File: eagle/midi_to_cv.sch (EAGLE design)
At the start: 49 parts, among them IC1 TL084P, IC2 TL084P, U1 ATMEGA328P_PDIP

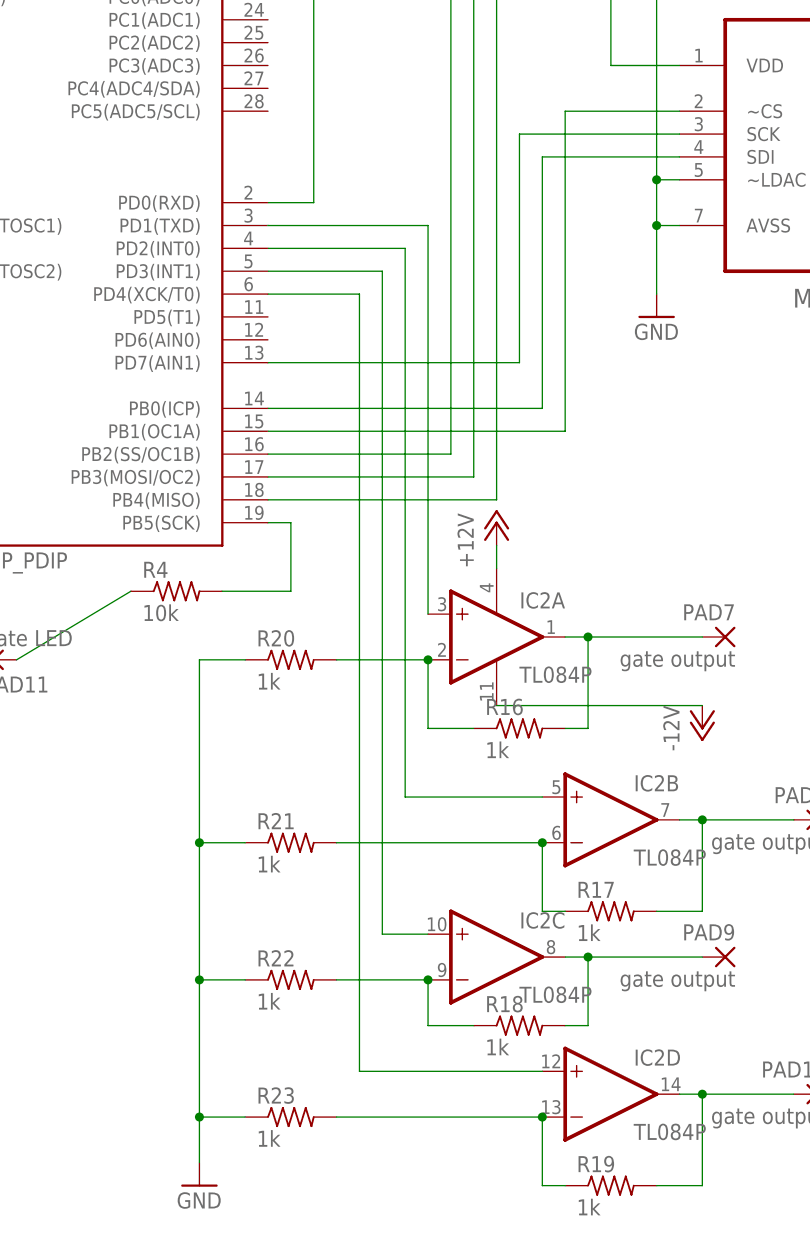
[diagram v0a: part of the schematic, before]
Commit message: routed with jumpers for gates and one via
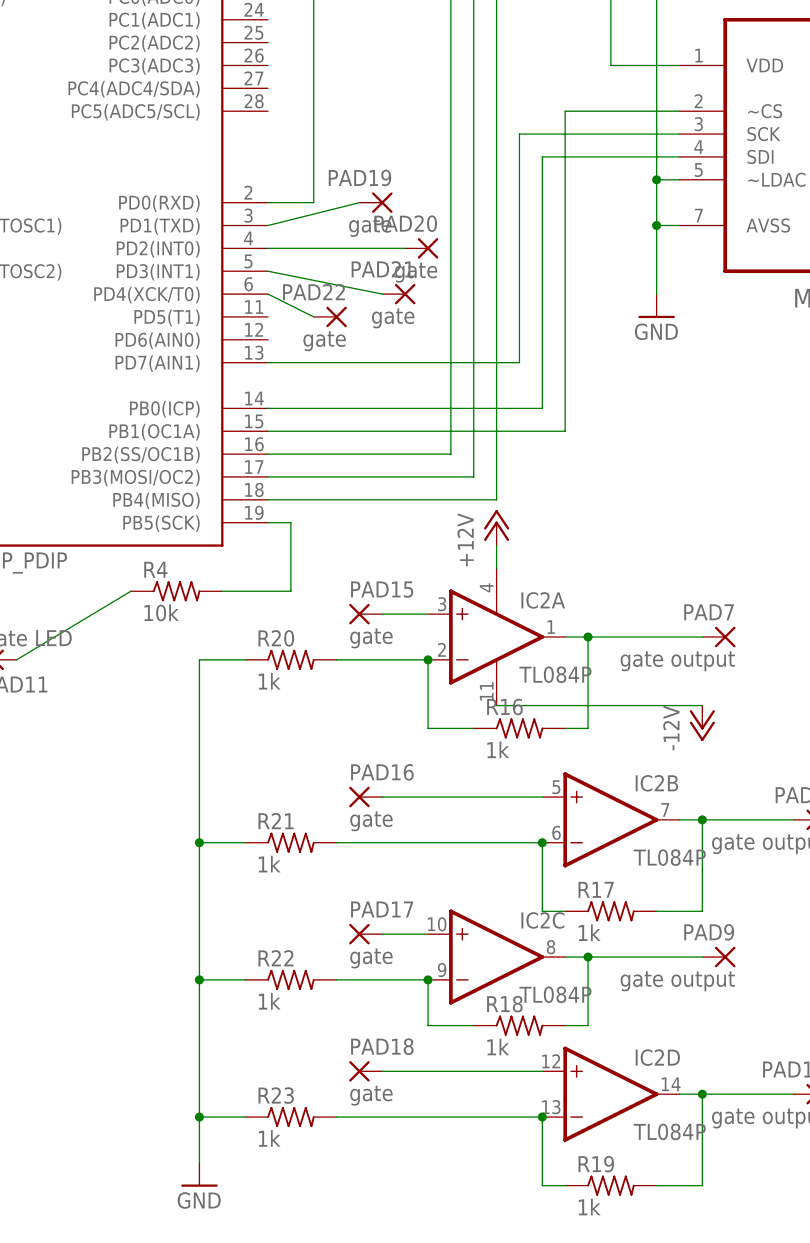
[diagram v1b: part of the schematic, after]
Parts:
- added PAD15, PAD16, PAD17, PAD18, PAD19, PAD20, PAD21, PAD22: gate, wirepad:2,54/0,9
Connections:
- new net N$43: PAD22.P, U1.PD4(XCK/T0)
- new net N$44: IC2C.+IN, PAD17.P
- new net N$45: IC2B.+IN, PAD16.P
- new net N$46: IC2A.+IN, PAD15.P
- net N$31: now also PAD19.P; no longer IC2A.+IN
- net N$32: now also PAD20.P; no longer IC2B.+IN
- net N$33: now also PAD21.P; no longer IC2C.+IN
- net N$34: now also PAD18.P; no longer U1.PD4(XCK/T0)
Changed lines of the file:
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@@
 <grid distance="0.1" unitdist="inch" unit="inch" style="lines" multiple="1" display="no" altdistance="0.01" altunitdist="inch" altunit="inch"/>
 <layers>
-<layer number="1" name="Top" color="4" fill="1" visible="yes" active="no"/>
-<layer number="16" name="Bottom" color="1" fill="1" visible="yes" active="no"/>
-<layer number="17" name="Pads" color="2" fill="1" visible="yes" active="no"/>
-<layer number="18" name="Vias" color="2" fill="1" visible="yes" active="no"/>
-<layer number="19" name="Unrouted" color="6" fill="1" visible="yes" active="no"/>
-<layer number="20" name="Dimension" color="15" fill="1" visible="yes" active="no"/>
-<layer number="21" name="tPlace" color="7" fill="1" visible="yes" active="no"/>
-<layer number="22" name="bPlace" color="7" fill="1" visible="yes" active="no"/>
-<layer number="23" name="tOrigins" color="15" fill="1" visible="yes" active="no"/>
-<layer number="24" name="bOrigins" color="15" fill="1" visible="yes" active="no"/>
-<layer number="25" name="tNames" color="7" fill="1" visible="yes" active="no"/>
-<layer number="26" name="bNames" color="7" fill="1" visible="yes" active="no"/>
-<layer number="27" name="tValues" color="7" fill="1" visible="yes" active="no"/>
-<layer number="28" name="bValues" color="7" fill="1" visible="yes" active="no"/>
+<layer number="1" name="Top" color="4" fill="1" visible="no" active="no"/>
+<layer number="16" name="Bottom" color="1" fill="1" visible="no" active="no"/>
+<layer number="17" name="Pads" color="2" fill="1" visible="no" active="no"/>
+<layer number="18" name="Vias" color="2" fill="1" visible="no" active="no"/>
+<layer number="19" name="Unrouted" color="6" fill="1" visible="no" active="no"/>
+<layer number="20" name="Dimension" color="15" fill="1" visible="no" active="no"/>
+<layer number="21" name="tPlace" color="7" fill="1" visible="no" active="no"/>
+<layer number="22" name="bPlace" color="7" fill="1" visible="no" active="no"/>
+<layer number="23" name="tOrigins" color="15" fill="1" visible="no" active="no"/>
+<layer number="24" name="bOrigins" color="15" fill="1" visible="no" active="no"/>
+<layer number="25" name="tNames" color="7" fill="1" visible="no" active="no"/>
+<layer number="26" name="bNames" color="7" fill="1" visible="no" active="no"/>
+<layer number="27" name="tValues" color="7" fill="1" visible="no" active="no"/>
+<layer number="28" name="bValues" color="7" fill="1" visible="no" active="no"/>
 <layer number="29" name="tStop" color="7" fill="3" visible="no" active="no"/>
 <layer number="30" name="bStop" color="7" fill="6" visible="no" active="no"/>
@@
 <layer number="35" name="tGlue" color="7" fill="4" visible="no" active="no"/>
 <layer number="36" name="bGlue" color="7" fill="5" visible="no" active="no"/>
-<layer number="37" name="tTest" color="7" fill="1" visible="yes" active="no"/>
-<layer number="38" name="bTest" color="7" fill="1" visible="yes" active="no"/>
+<layer number="37" name="tTest" color="7" fill="1" visible="no" active="no"/>
+<layer number="38" name="bTest" color="7" fill="1" visible="no" active="no"/>
 <layer number="39" name="tKeepout" color="4" fill="11" visible="no" active="no"/>
 <layer number="40" name="bKeepout" color="1" fill="11" visible="no" active="no"/>
@@
 <layer number="44" name="Drills" color="7" fill="1" visible="no" active="no"/>
 <layer number="45" name="Holes" color="7" fill="1" visible="no" active="no"/>
-<layer number="46" name="Milling" color="3" fill="1" visible="yes" active="no"/>
-<layer number="47" name="Measures" color="7" fill="1" visible="yes" active="no"/>
-<layer number="48" name="Document" color="7" fill="1" visible="yes" active="no"/>
-<layer number="49" name="Reference" color="7" fill="1" visible="yes" active="no"/>
-<layer number="50" name="dxf" color="7" fill="1" visible="yes" active="no"/>
-<layer number="51" name="tDocu" color="7" fill="1" visible="yes" active="no"/>
-<layer number="52" name="bDocu" color="7" fill="1" visible="yes" active="no"/>
-<layer number="53" name="tGND_GNDA" color="7" fill="9" visible="yes" active="no"/>
-<layer number="54" name="bGND_GNDA" color="1" fill="9" visible="yes" active="no"/>
-<layer number="56" name="wert" color="7" fill="1" visible="yes" active="no"/>
-<layer number="57" name="tCAD" color="7" fill="1" visible="yes" active="no"/>
+<layer number="46" name="Milling" color="3" fill="1" visible="no" active="no"/>
+<layer number="47" name="Measures" color="7" fill="1" visible="no" active="no"/>
+<layer number="48" name="Document" color="7" fill="1" visible="no" active="no"/>
+<layer number="49" name="Reference" color="7" fill="1" visible="no" active="no"/>
+<layer number="50" name="dxf" color="7" fill="1" visible="no" active="no"/>
+<layer number="51" name="tDocu" color="7" fill="1" visible="no" active="no"/>
+<layer number="52" name="bDocu" color="7" fill="1" visible="no" active="no"/>
+<layer number="53" name="tGND_GNDA" color="7" fill="9" visible="no" active="no"/>
+<layer number="54" name="bGND_GNDA" color="1" fill="9" visible="no" active="no"/>
+<layer number="56" name="wert" color="7" fill="1" visible="no" active="no"/>
+<layer number="57" name="tCAD" color="7" fill="1" visible="no" active="no"/>
 <layer number="90" name="Modules" color="5" fill="1" visible="yes" active="yes"/>
 <layer number="91" name="Nets" color="2" fill="1" visible="yes" active="yes"/>
@@
 <part name="P+7" library="supply1" deviceset="+12V" device=""/>
 <part name="P+8" library="supply1" deviceset="+12V" device=""/>
+<part name="PAD15" library="wirepad" deviceset="2,54/0,9" device="" value="gate"/>
+<part name="PAD16" library="wirepad" deviceset="2,54/0,9" device="" value="gate"/>
+<part name="PAD17" library="wirepad" deviceset="2,54/0,9" device="" value="gate"/>
+<part name="PAD18" library="wirepad" deviceset="2,54/0,9" device="" value="gate"/>
+<part name="PAD19" library="wirepad" deviceset="2,54/0,9" device="" value="gate"/>
+<part name="PAD20" library="wirepad" deviceset="2,54/0,9" device="" value="gate"/>
+<part name="PAD21" library="wirepad" deviceset="2,54/0,9" device="" value="gate"/>
+<part name="PAD22" library="wirepad" deviceset="2,54/0,9" device="" value="gate"/>
 </parts>
 <sheets>
@@
 <instance part="P+8" gate="1" x="68.58" y="15.24"/>
 <instance part="IC2" gate="P" x="68.58" y="2.54"/>
+<instance part="PAD15" gate="1" x="53.34" y="5.08"/>
+<instance part="PAD16" gate="1" x="53.34" y="-15.24"/>
+<instance part="PAD17" gate="1" x="53.34" y="-30.48"/>
+<instance part="PAD18" gate="1" x="53.34" y="-45.72"/>
+<instance part="PAD19" gate="1" x="55.88" y="50.8" rot="MR0"/>
+<instance part="PAD20" gate="1" x="60.96" y="45.72" rot="MR0"/>
+<instance part="PAD21" gate="1" x="58.42" y="40.64" rot="MR0"/>
+<instance part="PAD22" gate="1" x="50.8" y="38.1" rot="MR0"/>
 </instances>
 <busses>
@@
 <segment>
 <pinref part="U1" gate="G$1" pin="PD1(TXD)"/>
-<pinref part="IC2" gate="A" pin="+IN"/>
-<wire x1="43.18" y1="48.26" x2="60.96" y2="48.26" width="0.1524" layer="91"/>
-<wire x1="60.96" y1="48.26" x2="60.96" y2="5.08" width="0.1524" layer="91"/>
+<wire x1="43.18" y1="48.26" x2="53.34" y2="50.8" width="0.1524" layer="91"/>
+<pinref part="PAD19" gate="1" pin="P"/>
 </segment>
 </net>
@@
 <pinref part="U1" gate="G$1" pin="PD2(INT0)"/>
 <wire x1="43.18" y1="45.72" x2="58.42" y2="45.72" width="0.1524" layer="91"/>
-<wire x1="58.42" y1="45.72" x2="58.42" y2="-15.24" width="0.1524" layer="91"/>
-<pinref part="IC2" gate="B" pin="+IN"/>
-<wire x1="58.42" y1="-15.24" x2="73.66" y2="-15.24" width="0.1524" layer="91"/>
+<pinref part="PAD20" gate="1" pin="P"/>
 </segment>
 </net>
@@
 <segment>
 <pinref part="U1" gate="G$1" pin="PD3(INT1)"/>
-<wire x1="43.18" y1="43.18" x2="55.88" y2="43.18" width="0.1524" layer="91"/>
-<wire x1="55.88" y1="43.18" x2="55.88" y2="-30.48" width="0.1524" layer="91"/>
-<pinref part="IC2" gate="C" pin="+IN"/>
-<wire x1="55.88" y1="-30.48" x2="60.96" y2="-30.48" width="0.1524" layer="91"/>
+<wire x1="43.18" y1="43.18" x2="55.88" y2="40.64" width="0.1524" layer="91"/>
+<pinref part="PAD21" gate="1" pin="P"/>
 </segment>
 </net>
 <net name="N$34" class="0">
 <segment>
-<pinref part="U1" gate="G$1" pin="PD4(XCK/T0)"/>
-<wire x1="43.18" y1="40.64" x2="53.34" y2="40.64" width="0.1524" layer="91"/>
-<wire x1="53.34" y1="40.64" x2="53.34" y2="-45.72" width="0.1524" layer="91"/>
 <pinref part="IC2" gate="D" pin="+IN"/>
-<wire x1="53.34" y1="-45.72" x2="73.66" y2="-45.72" width="0.1524" layer="91"/>
+<wire x1="55.88" y1="-45.72" x2="73.66" y2="-45.72" width="0.1524" layer="91"/>
+<pinref part="PAD18" gate="1" pin="P"/>
 </segment>
 </net>
@@
 </segment>
 </net>
+<net name="N$43" class="0">
+<segment>
+<pinref part="U1" gate="G$1" pin="PD4(XCK/T0)"/>
+<wire x1="43.18" y1="40.64" x2="48.26" y2="38.1" width="0.1524" layer="91"/>
+<pinref part="PAD22" gate="1" pin="P"/>
+</segment>
+</net>
+<net name="N$44" class="0">
+<segment>
+<pinref part="IC2" gate="C" pin="+IN"/>
+<wire x1="55.88" y1="-30.48" x2="60.96" y2="-30.48" width="0.1524" layer="91"/>
+<pinref part="PAD17" gate="1" pin="P"/>
+</segment>
+</net>
+<net name="N$45" class="0">
+<segment>
+<pinref part="IC2" gate="B" pin="+IN"/>
+<wire x1="55.88" y1="-15.24" x2="73.66" y2="-15.24" width="0.1524" layer="91"/>
+<pinref part="PAD16" gate="1" pin="P"/>
+</segment>
+</net>
+<net name="N$46" class="0">
+<segment>
+<pinref part="PAD15" gate="1" pin="P"/>
+<pinref part="IC2" gate="A" pin="+IN"/>
+<wire x1="55.88" y1="5.08" x2="60.96" y2="5.08" width="0.1524" layer="91"/>
+</segment>
+</net>

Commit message: corrected to smaller xtal package
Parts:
- Q1: device crystal:CRYSTALHC33U-V -> crystal:CRYSTALHC49U-V
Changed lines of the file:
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@@
 <grid distance="0.1" unitdist="inch" unit="inch" style="lines" multiple="1" display="no" altdistance="0.01" altunitdist="inch" altunit="inch"/>
 <layers>
-<layer number="1" name="Top" color="4" fill="1" visible="no" active="no"/>
-<layer number="16" name="Bottom" color="1" fill="1" visible="no" active="no"/>
-<layer number="17" name="Pads" color="2" fill="1" visible="no" active="no"/>
-<layer number="18" name="Vias" color="2" fill="1" visible="no" active="no"/>
-<layer number="19" name="Unrouted" color="6" fill="1" visible="no" active="no"/>
-<layer number="20" name="Dimension" color="15" fill="1" visible="no" active="no"/>
-<layer number="21" name="tPlace" color="7" fill="1" visible="no" active="no"/>
-<layer number="22" name="bPlace" color="7" fill="1" visible="no" active="no"/>
-<layer number="23" name="tOrigins" color="15" fill="1" visible="no" active="no"/>
-<layer number="24" name="bOrigins" color="15" fill="1" visible="no" active="no"/>
-<layer number="25" name="tNames" color="7" fill="1" visible="no" active="no"/>
-<layer number="26" name="bNames" color="7" fill="1" visible="no" active="no"/>
-<layer number="27" name="tValues" color="7" fill="1" visible="no" active="no"/>
-<layer number="28" name="bValues" color="7" fill="1" visible="no" active="no"/>
+<layer number="1" name="Top" color="4" fill="1" visible="yes" active="no"/>
+<layer number="16" name="Bottom" color="1" fill="1" visible="yes" active="no"/>
+<layer number="17" name="Pads" color="2" fill="1" visible="yes" active="no"/>
+<layer number="18" name="Vias" color="2" fill="1" visible="yes" active="no"/>
+<layer number="19" name="Unrouted" color="6" fill="1" visible="yes" active="no"/>
+<layer number="20" name="Dimension" color="15" fill="1" visible="yes" active="no"/>
+<layer number="21" name="tPlace" color="7" fill="1" visible="yes" active="no"/>
+<layer number="22" name="bPlace" color="7" fill="1" visible="yes" active="no"/>
+<layer number="23" name="tOrigins" color="15" fill="1" visible="yes" active="no"/>
+<layer number="24" name="bOrigins" color="15" fill="1" visible="yes" active="no"/>
+<layer number="25" name="tNames" color="7" fill="1" visible="yes" active="no"/>
+<layer number="26" name="bNames" color="7" fill="1" visible="yes" active="no"/>
+<layer number="27" name="tValues" color="7" fill="1" visible="yes" active="no"/>
+<layer number="28" name="bValues" color="7" fill="1" visible="yes" active="no"/>
 <layer number="29" name="tStop" color="7" fill="3" visible="no" active="no"/>
 <layer number="30" name="bStop" color="7" fill="6" visible="no" active="no"/>
@@
 <layer number="35" name="tGlue" color="7" fill="4" visible="no" active="no"/>
 <layer number="36" name="bGlue" color="7" fill="5" visible="no" active="no"/>
-<layer number="37" name="tTest" color="7" fill="1" visible="no" active="no"/>
-<layer number="38" name="bTest" color="7" fill="1" visible="no" active="no"/>
+<layer number="37" name="tTest" color="7" fill="1" visible="yes" active="no"/>
+<layer number="38" name="bTest" color="7" fill="1" visible="yes" active="no"/>
 <layer number="39" name="tKeepout" color="4" fill="11" visible="no" active="no"/>
 <layer number="40" name="bKeepout" color="1" fill="11" visible="no" active="no"/>
@@
 <layer number="44" name="Drills" color="7" fill="1" visible="no" active="no"/>
 <layer number="45" name="Holes" color="7" fill="1" visible="no" active="no"/>
-<layer number="46" name="Milling" color="3" fill="1" visible="no" active="no"/>
-<layer number="47" name="Measures" color="7" fill="1" visible="no" active="no"/>
-<layer number="48" name="Document" color="7" fill="1" visible="no" active="no"/>
-<layer number="49" name="Reference" color="7" fill="1" visible="no" active="no"/>
-<layer number="50" name="dxf" color="7" fill="1" visible="no" active="no"/>
-<layer number="51" name="tDocu" color="7" fill="1" visible="no" active="no"/>
-<layer number="52" name="bDocu" color="7" fill="1" visible="no" active="no"/>
-<layer number="53" name="tGND_GNDA" color="7" fill="9" visible="no" active="no"/>
-<layer number="54" name="bGND_GNDA" color="1" fill="9" visible="no" active="no"/>
-<layer number="56" name="wert" color="7" fill="1" visible="no" active="no"/>
-<layer number="57" name="tCAD" color="7" fill="1" visible="no" active="no"/>
+<layer number="46" name="Milling" color="3" fill="1" visible="yes" active="no"/>
+<layer number="47" name="Measures" color="7" fill="1" visible="yes" active="no"/>
+<layer number="48" name="Document" color="7" fill="1" visible="yes" active="no"/>
+<layer number="49" name="Reference" color="7" fill="1" visible="yes" active="no"/>
+<layer number="50" name="dxf" color="7" fill="1" visible="yes" active="no"/>
+<layer number="51" name="tDocu" color="7" fill="1" visible="yes" active="no"/>
+<layer number="52" name="bDocu" color="7" fill="1" visible="yes" active="no"/>
+<layer number="53" name="tGND_GNDA" color="7" fill="9" visible="yes" active="no"/>
+<layer number="54" name="bGND_GNDA" color="1" fill="9" visible="yes" active="no"/>
+<layer number="56" name="wert" color="7" fill="1" visible="yes" active="no"/>
+<layer number="57" name="tCAD" color="7" fill="1" visible="yes" active="no"/>
 <layer number="90" name="Modules" color="5" fill="1" visible="yes" active="yes"/>
 <layer number="91" name="Nets" color="2" fill="1" visible="yes" active="yes"/>
@@
 <part name="U1" library="SparkFun-DigitalIC" deviceset="ATMEGA328P_PDIP" device=""/>
 <part name="U$1" library="eurorack" deviceset="POWER" device=""/>
-<part name="Q1" library="crystal" deviceset="CRYSTAL" device="HC33U-V"/>
+<part name="Q1" library="crystal" deviceset="CRYSTAL" device="HC49U-V"/>
 <part name="C1" library="rcl" deviceset="C-US" device="025-040X050" value="27pF"/>
 <part name="C2" library="rcl" deviceset="C-US" device="025-040X050" value="27pF"/>
